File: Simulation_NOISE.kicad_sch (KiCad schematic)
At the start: 2 parts

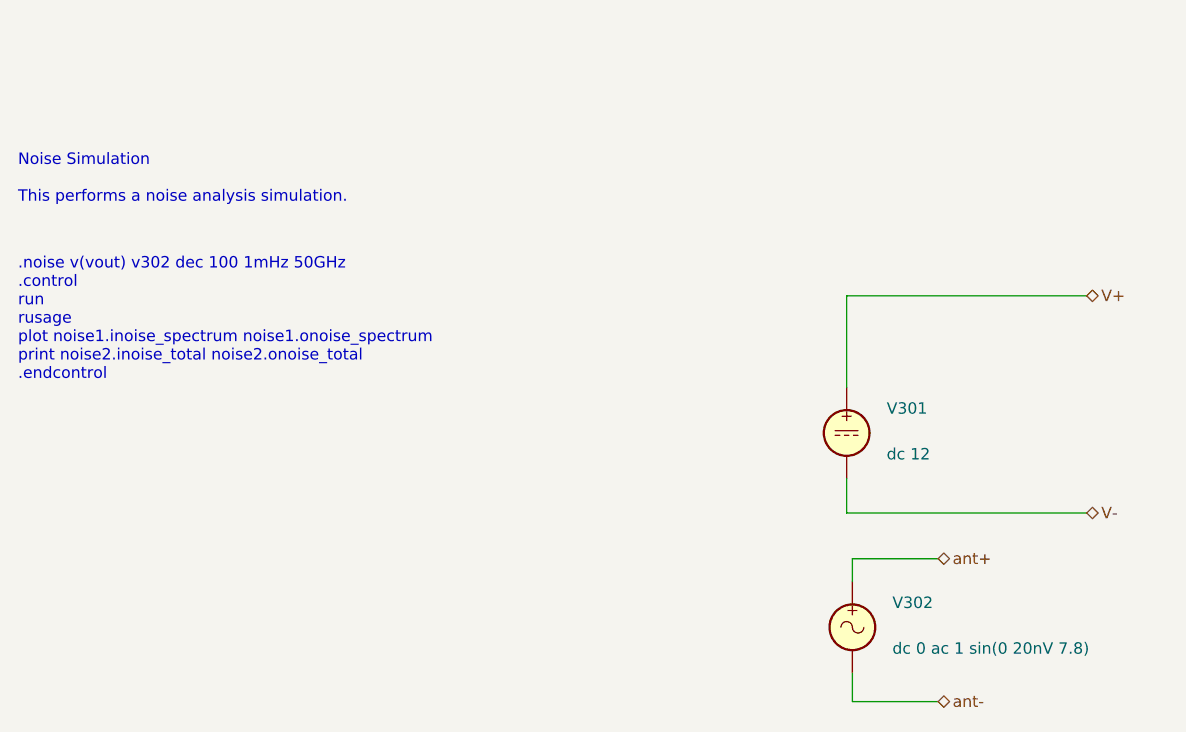
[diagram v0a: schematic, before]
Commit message: Fix simulation primitives and document simulation types
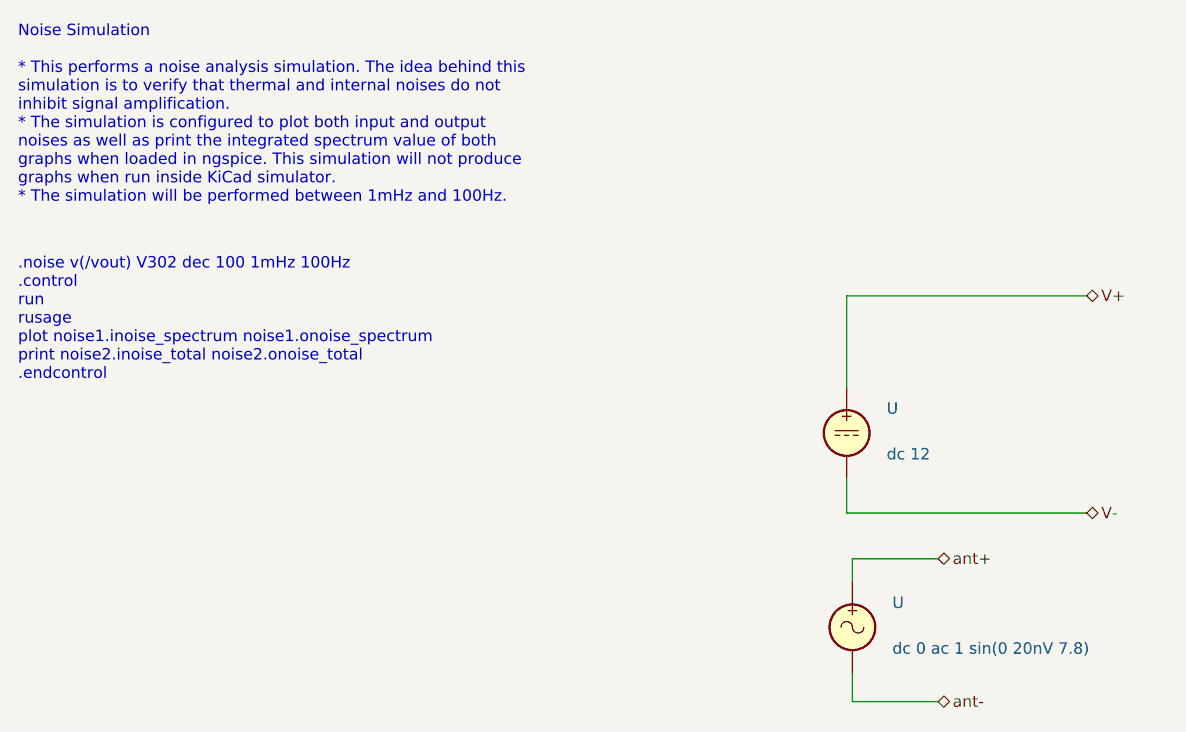
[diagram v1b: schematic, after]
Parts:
- U: renamed from V301; value ~ -> (none)
- U: renamed from V302; value ~ -> (none)
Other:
- note added: ".noise v(/vout) V302 dec 100 1mHz 100Hz .control run rusage plot noise1.inoise_spectrum noise1.onoise_spectrum print noise2.inoise_total noise2.onoise_total .endcontrol"
- note added: "Noise Simulation * This performs a noise analysis simulation. The idea behind this simulation is to verify that thermal and internal noises do not inhibit signal amplification. * The simulation is configured to plot both input and output noises as well as print the integrated spectrum value of both graphs when loaded in ngspice. This simulation will not produce graphs when run inside KiCad simula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"
- note removed: ".noise v(vout) v302 dec 100 1mHz 50GHz .control run rusage plot noise1.inoise_spectrum noise1.onoise_spectrum print noise2.inoise_total noise2.onoise_total .endcontrol"
- note removed: "Noise Simulation This performs a noise analysis simulation."
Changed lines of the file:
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@@
-(kicad_sch (version 20211123) (generator eeschema)
+(kicad_sch (version 20220404) (generator eeschema)
   (paper "A4")
   (wire (pts (xy 155.575 85.725) (xy 155.575 89.535))
-    (stroke (width 0) (type default) (color 0 0 0 0))
+    (stroke (width 0) (type default))
   )
   (wire (pts (xy 156.21 110.49) (xy 165.735 110.49))
-    (stroke (width 0) (type default) (color 0 0 0 0))
+    (stroke (width 0) (type default))
   )
   (wire (pts (xy 156.21 97.155) (xy 156.21 94.615))
-    (stroke (width 0) (type default) (color 0 0 0 0))
+    (stroke (width 0) (type default))
   )
   (wire (pts (xy 156.21 107.315) (xy 156.21 110.49))
-    (stroke (width 0) (type default) (color 0 0 0 0))
+    (stroke (width 0) (type default))
   )
   (wire (pts (xy 155.575 65.405) (xy 155.575 75.565))
-    (stroke (width 0) (type default) (color 0 0 0 0))
+    (stroke (width 0) (type default))
   )
   (wire (pts (xy 156.21 94.615) (xy 165.735 94.615))
-    (stroke (width 0) (type default) (color 0 0 0 0))
+    (stroke (width 0) (type default))
   )
   (wire (pts (xy 155.575 89.535) (xy 182.245 89.535))
-    (stroke (width 0) (type default) (color 0 0 0 0))
+    (stroke (width 0) (type default))
   )
   (wire (pts (xy 155.575 65.405) (xy 182.245 65.405))
-    (stroke (width 0) (type default) (color 0 0 0 0))
+    (stroke (width 0) (type default))
   )
-  (text "Noise Simulation\n\nThis performs a noise analysis simulation."
+  (text "Noise Simulation\n\n* This performs a noise analysis simulation. The idea behind this\nsimulation is to verify that thermal and internal noises do not\ninhibit signal amplification.\n* The simulation is configured to plot both input and output\nnoises as well as print the integrated spectrum value of both\ngraphs when loaded in ngspice. This simulation will not produce\ngraphs when run inside KiCad simulator.\n* The simulation will be performed between 1mHz and 100Hz."
     (at 63.5 55.245 0)
     (effects (font (size 1.27 1.27)) (justify left bottom))
   )
-  (text ".noise v(vout) v302 dec 100 1mHz 50GHz\n.control\nrun\nrusage\nplot noise1.inoise_spectrum noise1.onoise_spectrum\nprint noise2.inoise_total noise2.onoise_total\n.endcontrol"
+  (text ".noise v(/vout) V302 dec 100 1mHz 100Hz\n.control\nrun\nrusage\nplot noise1.inoise_spectrum noise1.onoise_spectrum\nprint noise2.inoise_total noise2.onoise_total\n.endcontrol"
     (at 63.5 74.93 0)
     (effects (font (size 1.27 1.27)) (justify left bottom))
   )
-  (hierarchical_label "ant-" (shape bidirectional) (at 165.735 110.49 0)
+  (hierarchical_label "ant-" (shape bidirectional) (at 165.735 110.49 0) (fields_autoplaced)
     (effects (font (size 1.27 1.27)) (justify left))
   )
-  (hierarchical_label "V-" (shape bidirectional) (at 182.245 89.535 0)
+  (hierarchical_label "V-" (shape bidirectional) (at 182.245 89.535 0) (fields_autoplaced)
     (effects (font (size 1.27 1.27)) (justify left))
   )
-  (hierarchical_label "ant+" (shape bidirectional) (at 165.735 94.615 0)
+  (hierarchical_label "ant+" (shape bidirectional) (at 165.735 94.615 0) (fields_autoplaced)
     (effects (font (size 1.27 1.27)) (justify left))
   )
-  (hierarchical_label "V+" (shape bidirectional) (at 182.245 65.405 0)
+  (hierarchical_label "V+" (shape bidirectional) (at 182.245 65.405 0) (fields_autoplaced)
     (effects (font (size 1.27 1.27)) (justify left))
   )
   (symbol (lib_id "Simulation_SPICE:VDC") (at 155.575 80.645 0) (unit 1)
     (in_bom yes) (on_board yes) (fields_autoplaced)
-    (property "Reference" "V301" (id 0) (at 160.02 77.9151 0)
+    (default_instance (reference "U") (unit 1) (value "") (footprint ""))
+    (property "Reference" "U" (id 0) (at 160.02 77.9151 0)
       (effects (font (size 1.27 1.27)) (justify left))
     )
-    (property "Value" "~" (id 1) (at 160.02 80.4551 0)
+    (property "Value" "" (id 1) (at 160.02 80.4551 0)
       (effects (font (size 1.27 1.27)) (justify left))
     )
@@
   (symbol (lib_id "Simulation_SPICE:VSIN") (at 156.21 102.235 0) (unit 1)
     (in_bom yes) (on_board yes) (fields_autoplaced)
-    (property "Reference" "V302" (id 0) (at 160.655 99.5051 0)
+    (default_instance (reference "U") (unit 1) (value "") (footprint ""))
+    (property "Reference" "U" (id 0) (at 160.655 99.5051 0)
       (effects (font (size 1.27 1.27)) (justify left))
     )
-    (property "Value" "~" (id 1) (at 160.655 102.0451 0)
+    (property "Value" "" (id 1) (at 160.655 102.0451 0)
       (effects (font (size 1.27 1.27)) (justify left))
     )
